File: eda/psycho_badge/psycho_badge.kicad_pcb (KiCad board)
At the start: 2 copper layers, 152.4 x 101.6 mm, 53 parts, among them J1 Battery_Conn, J21 01x02, J22 01x02, SW1 SW_SPDT_SS12D00G, U1 ESP32-WEMOS-LOLIN32-LITE

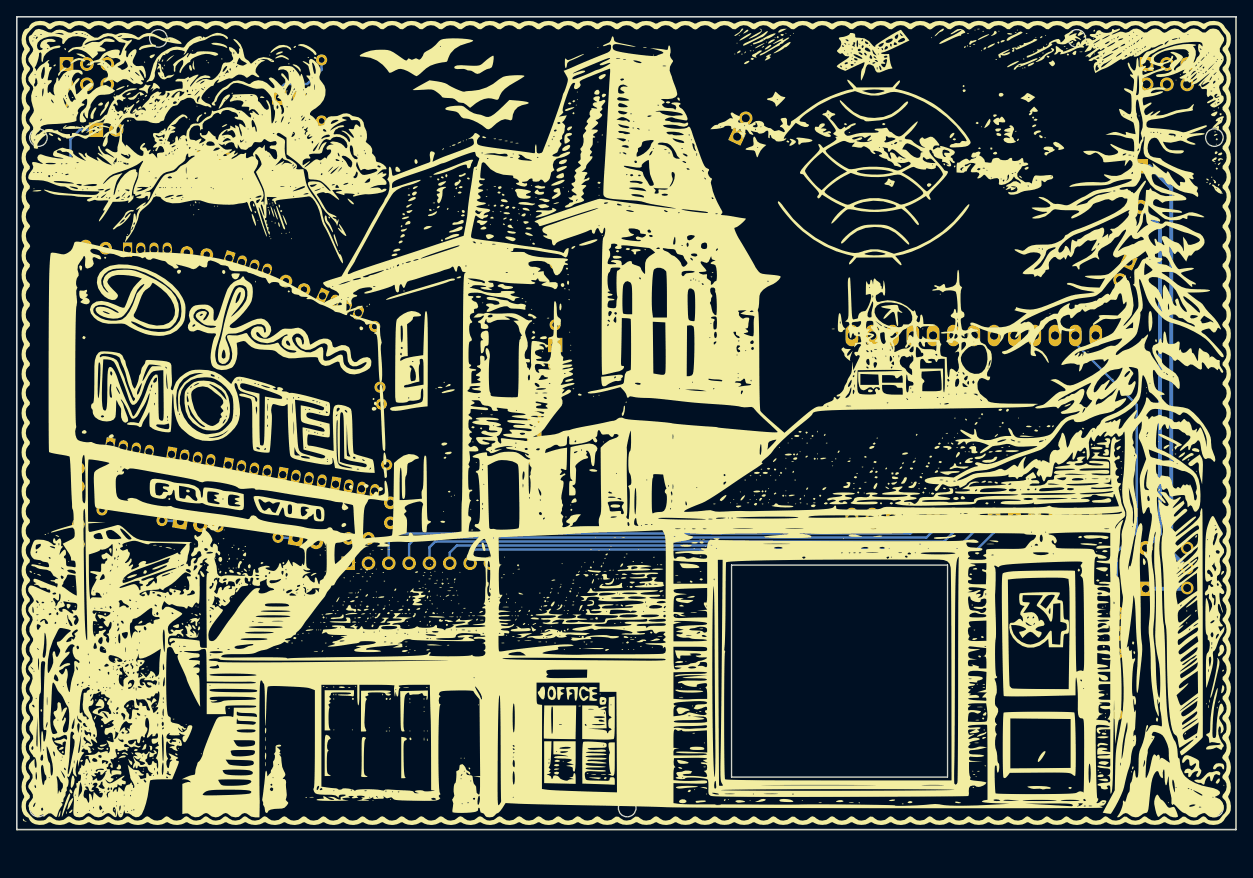
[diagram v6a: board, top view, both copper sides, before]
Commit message: main pcb complete
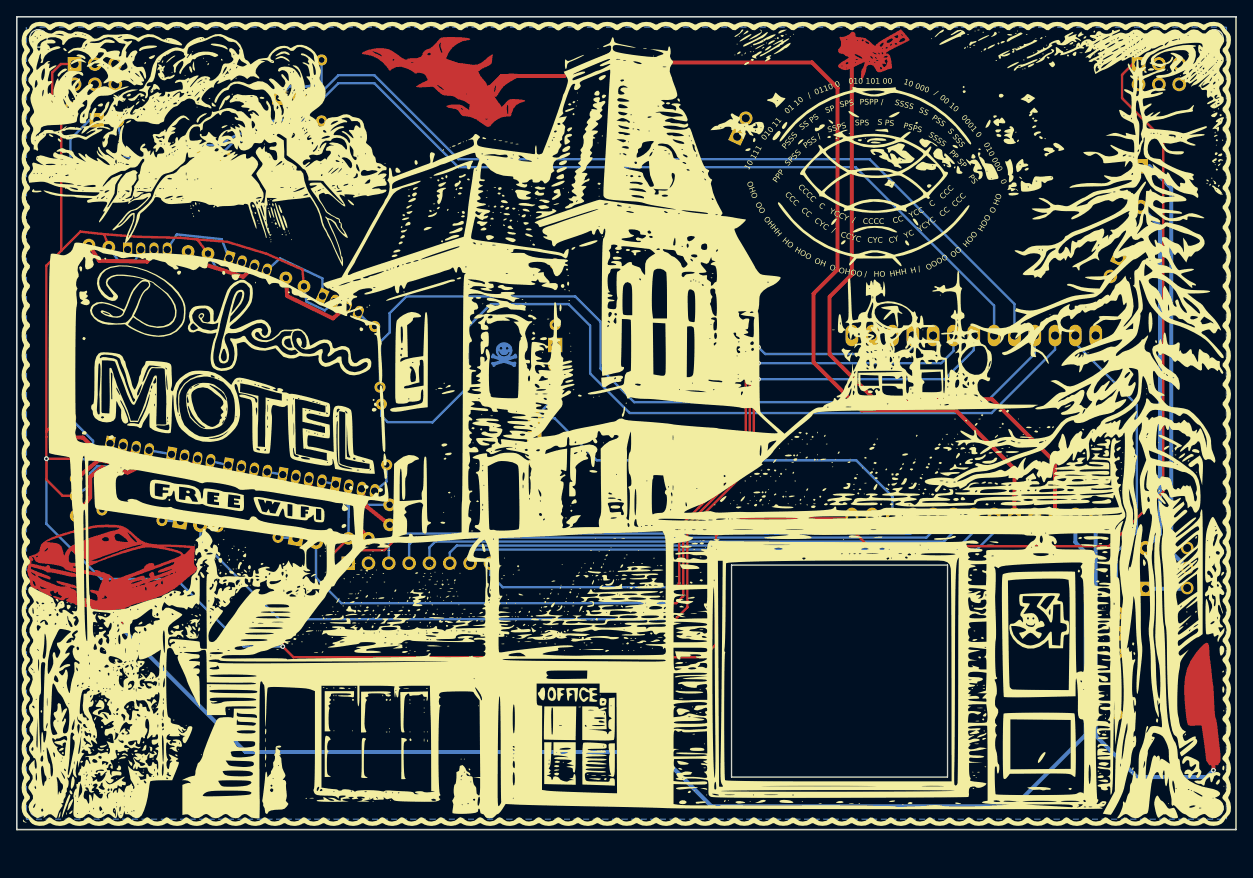
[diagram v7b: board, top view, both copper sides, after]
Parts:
- removed the REF** at (214.0, 51.8)
- removed the REF** at (67.0, 51.8)
- removed the REF** at (140.6, 135.6)
- added Fold: LED_Fold_Indicator_1, 0_local:LED_Fold_Indicator_back, F.Cu at (81.2, 102.9)
- added Fold: LED_Fold_Indicator_1, 0_local:LED_Fold_Indicator_back, F.Cu at (197.7, 114.2)
- added Fold: LED_Fold_Indicator_1, 0_local:LED_Fold_Indicator_back, F.Cu at (136.2, 81.3)
- added Fold: LED_Fold_Indicator_1, 0_local:LED_Fold_Indicator_back, F.Cu at (97.4, 66.0)
- added Fold: LED_Fold_Indicator_1, 0_local:LED_Fold_Indicator_back, F.Cu at (109.2, 71.3)
- added Fold: LED_Fold_Indicator_1, 0_local:LED_Fold_Indicator_back, F.Cu at (76.8, 94.9)
- added Fold: LED_Fold_Indicator_1, 0_local:LED_Fold_Indicator_back, F.Cu at (84.5, 63.1)
- added Fold: LED_Fold_Indicator_1, 0_local:LED_Fold_Indicator_back, F.Cu at (124.3, 90.1)
- added Fold: LED_Fold_Indicator_1, 0_local:LED_Fold_Indicator_back, F.Cu at (95.5, 105.1)
- added G***: LOGO, 0_alt_bier:logo-alt_bier-1100dpi-8x21mm-back, F.Cu at (135.4, 54.4)
- added G-FMask: LOGO, 0_badge:psycho_badge_top_art_fmsk, F.Cu at (140.6, 87.7)
- added REF**: LED_4Pin_Indicator_Right_back, 0_local:LED_4Pin_Indicator_Right_back, F.Cu at (83.5, 62.5)
- added REF**: LED_2Pin_Indicator_back, 0_local:LED_2Pin_Indicator_back, F.Cu at (88.9, 60.9)
- added REF**: LED_2Pin_Indicator_Right_back, 0_local:LED_2Pin_Indicator_Right_back, F.Cu at (97.1, 105.4)
- added REF**: LED_2Pin_Indicator_back, 0_local:LED_2Pin_Indicator_back, F.Cu at (68.5, 49.5)
- added REF**: LED_4Pin_Indicator_back, 0_local:LED_4Pin_Indicator_back, F.Cu at (77.8, 95.6)
- added REF**: LED_4Pin_Indicator_Right_back, 0_local:LED_4Pin_Indicator_Right_back, F.Cu at (96.6, 64.9)
- added REF**: LED_4Pin_Indicator_Right_back, 0_local:LED_4Pin_Indicator_Right_back, F.Cu at (108.5, 70.3)
- added REF**: LED_2Pin_Indicator_Right_back, 0_local:LED_2Pin_Indicator_Right_back, F.Cu at (82.8, 103.2)
- added REF**: LED_2Pin_Indicator_Right_back, 0_local:LED_2Pin_Indicator_Right_back, F.Cu at (197.7, 112.3)
- added REF**: LED_2Pin_Indicator_Right_back, 0_local:LED_2Pin_Indicator_Right_back, F.Cu at (136.2, 79.4)
- added REF**: LED_2Pin_Indicator_back, 0_local:LED_2Pin_Indicator_back, F.Cu at (95.4, 50.2)
- added REF**: LED_2Pin_Indicator_Right_back, 0_local:LED_2Pin_Indicator_Right_back, F.Cu at (124.3, 88.3)
- added TCH1: SYM_Touch_lg_x4, 0_badge:psycho_badge_top_art_fcu, F.Cu at (140.6, 87.7)
- moved REF** 17.2 mm to (214.0, 39.4)
- moved REF** 15.0 mm to (67.0, 39.4)
- moved C24 4.00 mm to (70.9, 86.8)
- moved C22 3.59 mm to (71.7, 96.6)
- moved C23 3.47 mm to (71.7, 91.9)
- moved C12 2.89 mm to (75.8, 65.5), turned to 174 degrees
- moved C11 2.65 mm to (88.2, 66.3), turned to 174 degrees
- moved C10 2.36 mm to (100.2, 70.4), turned to 155 degrees
- moved C20 2.25 mm to (110.9, 97.7), turned to -90 degrees
- moved J21 1.29 mm to (202.1, 66.8)
- moved D31 1.16 mm to (74.3, 49.6)
- moved JSAO1 1.00 mm to (207.0, 43.9)
- moved JSAO2 1.00 mm to (74.0, 43.9)
- moved D24 0.20 mm to (76.4, 90.1)
- moved G-Silk 0.12 mm to (140.6, 87.7)
- renumbered G*** to G-Silk
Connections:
- D1 pad 2: 32 -> 33
- D2 pad 2: 33 -> 32
- D31 pad 2: 25 -> 26
- D32 pad 2: 25 -> 26
- D4 pad 2: 26 -> 25
- R10 pad 2: 14 -> 27
- R20 pad 2: 27 -> 14
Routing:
- net +3.3V: track 0.00 -> 454.8 mm, vias 0 -> 2
- net 15: track 0.00 -> 164.7 mm, vias 0 -> 1
- net 26: track 0.00 -> 136.8 mm
- net 33: track 0.00 -> 129.9 mm, vias 0 -> 2
- net 4: track 0.00 -> 121.0 mm
- net 25: track 0.00 -> 115.4 mm
- net 32: track 0.00 -> 112.0 mm, vias 0 -> 2
- net 14: track 0.00 -> 110.7 mm
- net 27: track 0.00 -> 104.9 mm
- net GND: track 0.00 -> 103.3 mm
- net 34: track 0.00 -> 80.9 mm, vias 0 -> 2
- net 2: track 0.00 -> 80.4 mm
- net 19: track 0.00 -> 59.2 mm
- net 13: track 0.00 -> 46.3 mm, vias 0 -> 1
- net D11: track 0.00 -> 10.4 mm
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- added copper zone on B.Cu, net GND
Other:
- board text added: "101.6mm"
- board text added: "152.4mm"
- board text added: "36.5mm"

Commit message: main badge pcb updates
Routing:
- added copper zone on F.Cu, net GND
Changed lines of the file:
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@@
+		(net 3)
+		(net_name "GND")
+		(layer "F.Cu")
+		(name "gnd_fill")
+		(hatch edge 0.5)
+		(priority 1)
+		(connect_pads yes
+			(clearance 0.25)
+		)
+		(min_thickness 0.2)
+		(filled_areas_thickness no)
+		(fill yes
+			(thermal_gap 0.2)
+			(thermal_bridge_width 0.5)
+		)
+		(polygon
+			(pts
+				(xy 65.4 103.7) (xy 65.5 103.3) (xy 66.1 103.1) (xy 66.6 102.8) (xy 66.8 102.3) (xy 67.2 101.8)
+				(xy 67.9 101.4) (xy 69.4 100.8) (xy 70.8 100.4) (xy 72 100.1) (xy 73.2 99.9) (xy 76 99.7) (xy 77.3 99.8)
+				(xy 78.1 100) (xy 78.8 100.5) (xy 79.7 101.4) (xy 80.1 101.7) (xy 80.7 102) (xy 82.1 102.2) (xy 85.7 102.3)
+				(xy 87.2 102.4) (xy 87.1 103.8) (xy 87.1 104.7) (xy 87.4 105.1) (xy 87.5 105.6) (xy 87.4 106.1)
+				(xy 87.1 106.5) (xy 86.3 107.2) (xy 84.5 108.7) (xy 83.6 109.2) (xy 82.4 109.8) (xy 80.9 110.4)
+				(xy 79.7 110.7) (xy 78.6 111) (xy 78.4 111.4) (xy 78.4 112.8) (xy 78.5 113.2) (xy 78.5 113.6) (xy 78.4 114)
+				(xy 78.1 114.2) (xy 77.6 114.4) (xy 77.1 114.3) (xy 76.7 113.8) (xy 76.6 113.2) (xy 76.8 112.6)
+				(xy 77 112.3) (xy 77 111.4) (xy 76.2 111.5) (xy 74.7 111.4) (xy 73.4 111.2) (xy 71.9 110.9) (xy 70.8 110.6)
+				(xy 69.2 110.1) (xy 67.9 109.6) (xy 66.5 108.9) (xy 65.5 108.2) (xy 65.5 108.6) (xy 66.3 109.2)
+				(xy 67 109.6) (xy 68 110) (xy 69.1 110.4) (xy 70.7 110.9) (xy 72 111.2) (xy 73.8 111.6) (xy 74.7 111.7)
+				(xy 75.8 111.8) (xy 76.6 111.8) (xy 76.7 111.9) (xy 76.7 112.3) (xy 76.4 112.8) (xy 76.3 113.2)
+				(xy 76.4 113.8) (xy 76.7 114.3) (xy 77.1 114.6) (xy 77.6 114.7) (xy 78.2 114.5) (xy 78.5 114.3)
+				(xy 78.7 114) (xy 78.8 113.5) (xy 78.7 112.9) (xy 78.7 111.5) (xy 78.8 111.2) (xy 79.6 111) (xy 80.9 110.7)
+				(xy 82 110.3) (xy 83.2 109.7) (xy 84.8 108.8) (xy 87 107) (xy 87.5 106.5) (xy 87.8 106) (xy 87.8 105.5)
+				(xy 87.7 105) (xy 87.6 104.8) (xy 87.4 104.6) (xy 87.4 103.6) (xy 87.6 102.5) (xy 87.8 102.2) (xy 88.4 101.8)
+				(xy 89.4 101.4) (xy 89.7 101.1) (xy 89.5 101) (xy 88.9 100.8) (xy 88.5 101.4) (xy 88.1 101.7) (xy 87.6 102)
+				(xy 87.1 102.1) (xy 86.2 102.1) (xy 83.7 102) (xy 81.9 101.9) (xy 80.8 101.7) (xy 80.2 101.4) (xy 79.7 101)
+				(xy 78.7 100) (xy 78.4 99.8) (xy 77.9 99.6) (xy 77.4 99.5) (xy 76.2 99.4) (xy 75.7 99.4) (xy 75.5 99.2)
+				(xy 75.3 98.8) (xy 74.7 98.8) (xy 74.7 99.2) (xy 74.6 99.5) (xy 74.4 99.6) (xy 73.7 99.6) (xy 72.8 99.7)
+				(xy 72.4 99.6) (xy 72.1 99.6) (xy 71.5 99.7) (xy 71.4 100) (xy 70.6 100.2) (xy 69.2 100.6) (xy 68.4 100.9)
+				(xy 67 101.6) (xy 66.6 102.1) (xy 66.3 102.6) (xy 65.8 102.9) (xy 65.3 103.1) (xy 65.1 103.8) (xy 65 104.5)
+				(xy 64.9 105.5) (xy 64.9 107.1) (xy 65.1 108.1) (xy 65.5 108.6) (xy 65.5 108.2) (xy 65.3 108) (xy 65.1 107)
+				(xy 65.1 105.6)
+			)
+		)
+	)
+	(zone
 		(net 3)
 		(net_name "GND")
@@
 			(thermal_gap 0.2)
 			(thermal_bridge_width 0.5)
-			(hatch_thickness 1)
-			(hatch_gap 3)
+			(hatch_thickness 0.3)
+			(hatch_gap 1.5)
 			(hatch_orientation 45)
 			(hatch_border_algorithm hatch_thickness)
